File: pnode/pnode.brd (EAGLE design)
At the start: 50 x 23 mm, 39 parts, among them IC2 HTU21D, IC3 SI4012

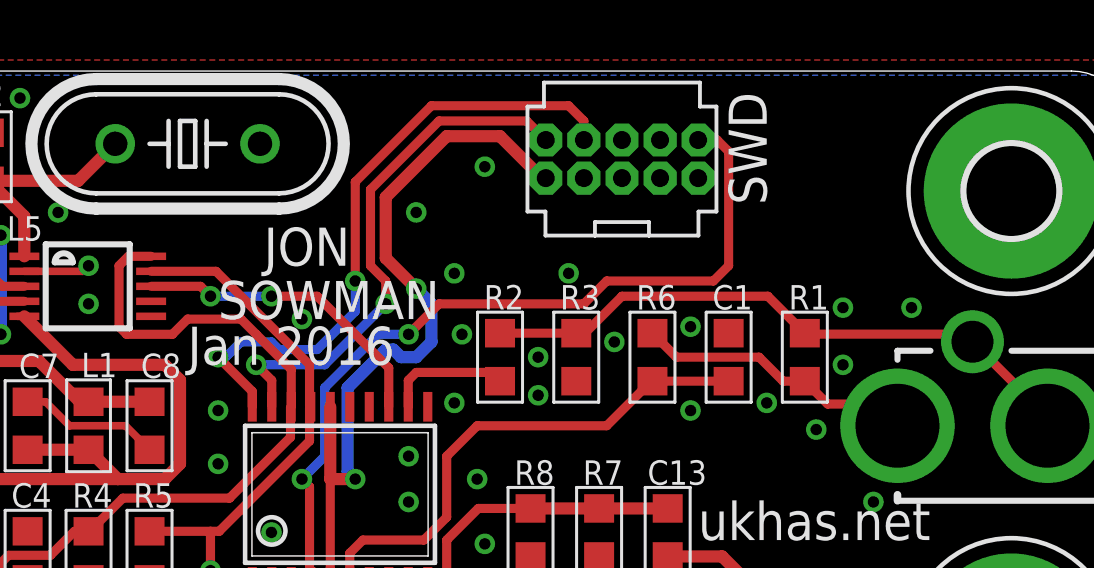
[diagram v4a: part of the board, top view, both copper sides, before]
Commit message: Added silk and submitted gerbers for pnodelv
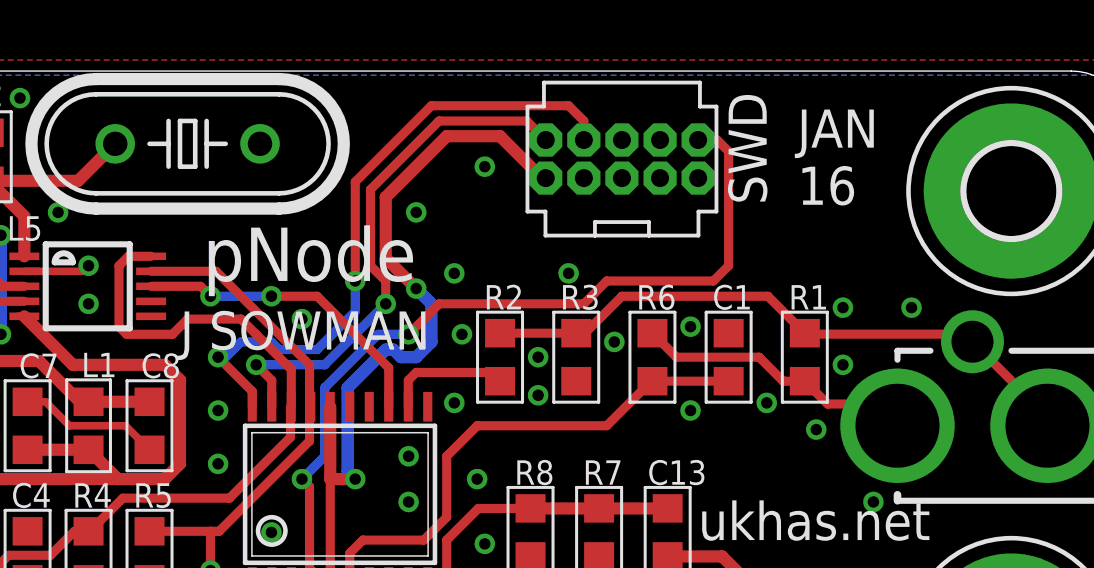
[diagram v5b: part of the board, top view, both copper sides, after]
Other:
- board text added: "J SOWMAN"
- board text added: "JAN 16"
- board text added: "jonsowman.com"
- board text added: "pNode"
- board text removed: "JON"
- board text removed: "Jan 2016"
- board text removed: "SOWMAN"
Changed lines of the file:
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@@
 <text x="9.144" y="0.508" size="1.27" layer="21" font="vector" ratio="15" rot="R90">UKHASnet</text>
 <text x="11.176" y="2.032" size="1.27" layer="21" font="vector" ratio="15" rot="R90">M0JSN</text>
-<text x="21.082" y="16.51" size="1.27" layer="21" font="vector" ratio="15">JON</text>
-<text x="19.558" y="14.732" size="1.27" layer="21" font="vector" ratio="15">SOWMAN</text>
-<text x="18.542" y="13.208" size="1.27" layer="21" font="vector" ratio="15">Jan 2016</text>
 <text x="35.56" y="7.366" size="1.27" layer="21" font="vector" ratio="15">ukhas.net</text>
 <text x="37.846" y="18.542" size="1.27" layer="21" font="vector" ratio="15" rot="R90">SWD</text>
 <text x="42.164" y="0.508" size="1.27" layer="21" font="vector" ratio="15" rot="R90">3.5-6V</text>
+<text x="19.05" y="16.002" size="1.778" layer="21" font="vector" ratio="15">pNode</text>
+<text x="18.288" y="13.716" size="1.27" layer="21" font="vector" ratio="15">J SOWMAN</text>
+<text x="38.862" y="18.542" size="1.27" layer="21" font="vector" ratio="15">JAN
+16</text>
+<text x="30.734" y="5.588" size="2.54" layer="22" font="vector" ratio="15" rot="MR0">pNode</text>
+<text x="33.782" y="1.778" size="2.54" layer="22" font="vector" ratio="15" rot="MR0">J SOWMAN</text>
+<text x="9.906" y="18.796" size="1.27" layer="22" font="vector" ratio="15" rot="MR270">jonsowman.com</text>
 </plain>
 <attributes>
@@
 </class>
 </classes>
-<designrules name="dirt_cheap_dirty_boards.v1 *">
+<designrules name="dirt_cheap_dirty_boards.v1">
 <description language="en">&lt;b&gt;Dirty Cheap Dirty Board Design Rules&lt;/b&gt;
 &lt;br&gt;
@@
 <param name="dpGapFactor" value="2.5"/>
 <param name="checkGrid" value="0"/>
-<param name="checkAngle" value="1"/>
+<param name="checkAngle" value="0"/>
 <param name="checkFont" value="1"/>
 <param name="checkRestrict" value="0"/>
@@
 </board>
 </drawing>
+<compatibility>
+<note version="6.3" minversion="6.2.2" severity="warning">
+Since Version 6.2.2 text objects can contain more than one line,
+which will not be processed correctly with this version.
+</note>
+</compatibility>
 </eagle>
